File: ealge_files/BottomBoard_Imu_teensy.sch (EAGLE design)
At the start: 96 parts, among them K1 MK20DX256VLH7, K2 MKL04Z32VLC4, T1 MCP1825S, U2 MPU-9250

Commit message: completed bottom layer.. and started with nanopi shield
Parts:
- removed J2: (no value), SparkFun-Connectors:M04PTH
- removed MICRO-USB: MINI-USB, t32_ref:MINI-USBMOLEX_0675031230
- removed SX10, SX11, SX12, SX13, SX14, SX15, SX16, SX17, SX18, SX19, SX2, SX20, SX21, SX22, SX23, SX24, SX25, SX26, SX27, SX28, SX29, SX3, SX30, SX31, SX32, SX33, SX34, SX35, SX36, SX37, SX38, SX39, SX4, SX40, SX41, SX42, SX43, SX44, SX45, SX46, SX47, SX48, SX49, SX5, SX50, SX51, SX52, SX53, SX54, SX55, SX56, SX57, SX58, SX59, SX6, SX60, SX7, SX8, SX9: PIN, t32_ref:PIN
- added D1: GREEN, SparkFun-LED:LED-GREEN0603
- added FLEX-RIBBON: 52207-0485, Molex_By_element14_Batch_1:52207-0485
- added R1: 100, SparkFun-Resistors:100OHM-0603-1/4W-5%
- added S2: (no value), SparkFun-Switches:SWITCH-SPDT-SMD-RIGHT-ANGLE
- added U1: 52207-0885, Molex_By_element14_Batch_1:52207-0885
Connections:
- removed net N$12: K1.RESET_B, K2.PTA4, K2.PTB5, SX38.P$1, SX56.P$1
- removed net N$16: MICRO-USB.3, R10.1
- removed net N$17: MICRO-USB.2, R7.1
- removed net N$18: C11.1, MICRO-USB.1, R14.1
- removed net N$19: K1.PTA1, K2.PTA6, MICRO-USB.4
- removed net N$22: K1.PTC1, SX6.P$1
- removed net N$23: K1.PTD6, SX7.P$1
- removed net N$24: K1.PTD5, SX8.P$1
- removed net N$25: K1.PTB2, SX9.P$1
- removed net N$26: K1.PTB3, SX10.P$1
- removed net N$27: K1.PTB1, SX11.P$1
- removed net N$28: K1.PTB0, SX13.P$1
- removed net N$29: K1.PTC0, SX15.P$1
- removed net N$30: K1.PTD1, SX17.P$1
- removed net N$31: K1.PTC5, P1.+, SX18.P$1
- removed net N$32: K1.PTC7, SX19.P$1
- removed net N$33: K1.PTC6, SX20.P$1
- removed net N$34: K1.PTC4, SX21.P$1
- removed net N$35: K1.PTC3, SX22.P$1
- removed net N$36: K1.PTD3, SX23.P$1
- removed net N$37: K1.PTD2, SX24.P$1
- removed net N$38: K1.PTD4, SX25.P$1
- removed net N$39: K1.PTD7, SX26.P$1
- removed net N$40: K1.PTA13, SX27.P$1
- removed net N$41: K1.PTA12, SX28.P$1
- removed net N$42: K1.PTD0, SX29.P$1
- removed net N$43: K1.PTB17, SX30.P$1
- removed net N$44: K1.PTB16, SX31.P$1
- removed net N$45: K1.ADC0_DM3, SX33.P$1
- removed net N$46: K1.PTA4, SX35.P$1
- removed net N$47: K1.PTB18, SX36.P$1
- removed net N$48: K1.PTE0, SX37.P$1
- removed net N$49: K1.PTC11, SX39.P$1
- removed net N$50: K1.PTC10, SX41.P$1
- removed net N$51: K1.PTC8, SX43.P$1
- removed net N$54: K1.DAC0, SX52.P$1
- removed net N$55: K1.ADC0_DP3, SX51.P$1
- removed net N$57: K1.PTA5, SX49.P$1
- removed net N$58: K1.PTB19, SX48.P$1
- removed net N$59: K1.PTE1, SX47.P$1
- removed net N$60: K1.PTC9, SX45.P$1
- removed net N$63: R13.2, SX46.P$1
- removed net N$64: K1.ADC0_DM0, SX12.P$1
- removed net N$65: K1.ADC0_DP0, SX14.P$1
- removed net N$69: C10.1, C12.1, C5.1, C6.1, K1.VDD@3, K1.VDD@30, K1.VDD@48, K1.VOUT33, K2.VDD, K2.VREFH, R12.2, R13.1, SX34.P$1, SX4.P$1, SX44.P$1, SX54.P$1, T1.OUT
- new net ID: K1.PTA1, K2.PTA6, U1.4
- new net N$4: D1.C, R1.1
- new net USB_DM: R7.1, U1.2
- new net USB_DP: R10.1, U1.3
- new net VCC: C4.1, S2.O
- new net V_MICRO_USB: C11.1, R14.1, U1.1
- net GND: now also FLEX-RIBBON.4, FLEX-RIBBON.5, FLEX-RIBBON.6, R1.2, S2.S, U1.10, U1.5, U1.6, U1.7, U1.8, U1.9; no longer J2.4, MICRO-USB.5, MICRO-USB.CASE, SX32.P$1, SX42.P$1, SX50.P$1, SX53.P$1, SX55.P$1, SX60.P$1
- net N$1: now also K1.RESET_B, K2.PTA4, K2.PTB5; no longer K2.PTA3, SX59.P$1
- net N$13: no longer SX16.P$1
- net N$2: no longer SX58.P$1
- net N$21: now also K1.PTC5, P1.+; no longer K1.PTC2, SX5.P$1
- net N$53: no longer SX3.P$1
- net N$61: no longer SX2.P$1
- net N$70: no longer SX57.P$1
- net N$9: no longer SX40.P$1
- net SCL/SCLK: now also FLEX-RIBBON.2, K1.PTB2; no longer J2.1
- net SDA/SDI: now also FLEX-RIBBON.3, K1.PTB3; no longer J2.2
- net VDD: now also C10.1, C12.1, C5.1, C6.1, K1.VDD@3, K1.VDD@30, K1.VDD@48, K1.VOUT33, K2.VDD, K2.VREFH, R12.2, R13.1, T1.OUT; no longer C4.1, J2.3, U2.VDD, U2.VDDIO
- net VDDIO: now also D1.A, FLEX-RIBBON.1, S2.P, U2.VDD, U2.VDDIO
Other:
- note removed: "0"
- note removed: "1"
- note removed: "10"
- note removed: "11"
- note removed: "12"
- note removed: "14 / A0"
- note removed: "15 / A1"
- note removed: "16 / A2"
- note removed: "17 / A3"
- note removed: "2"
- note removed: "20 / A6"
- note removed: "21 / A7"
- note removed: "22 / A8"
- note removed: "23 / A9"
- note removed: "24"
- note removed: "25"
- note removed: "26"
- note removed: "27"
- note removed: "28"
- note removed: "29"
- note removed: "3"
- note removed: "30"
- note removed: "31"
- note removed: "32"
- note removed: "33"
- note removed: "4"
- note removed: "5"
- note removed: "6"
- note removed: "7"
- note removed: "8"
- note removed: "9"
- note removed: "A10"
- note removed: "A11"
- note removed: "A12"
- note removed: "A13"
- note removed: "AREF"
- note removed: "DAC / A14"
- note removed: "EN'"
- note removed: "GND"
- note removed: "PROG"
- note removed: "RESET"
- note removed: "SWC"
- note removed: "SWD"
- note removed: "VBAT"
- moved on the sheet: C11, C16, C3, C4, P1, R4, R5, R6, R9, SJ2, T1, U2

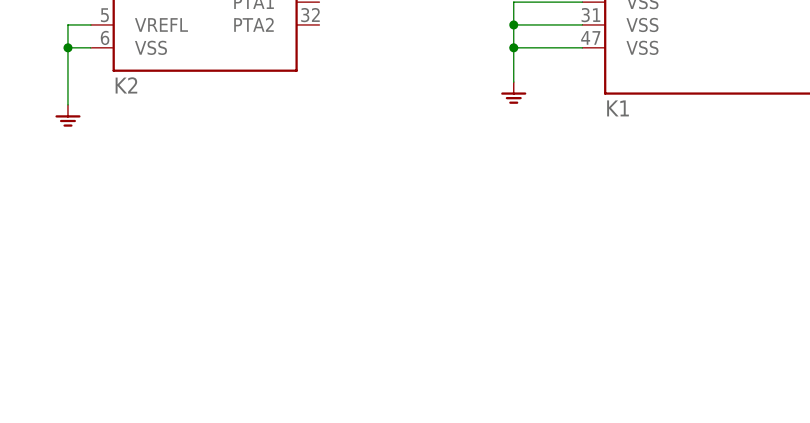
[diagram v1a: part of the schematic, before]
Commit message: added few libraries and completed all schematic
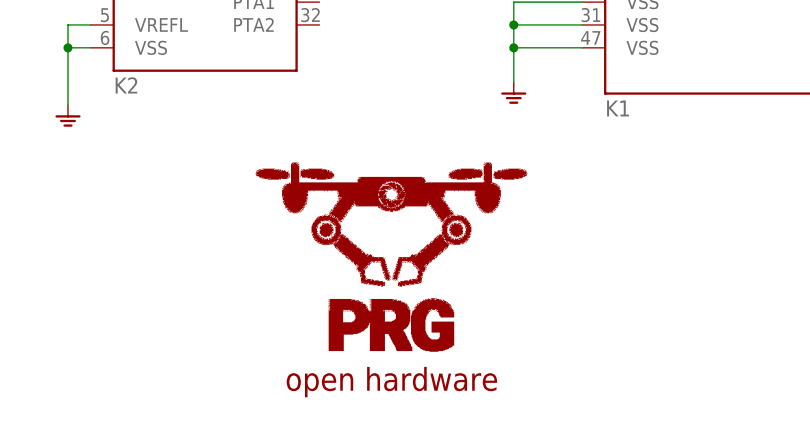
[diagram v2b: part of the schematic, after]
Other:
- note added: "open hardware"

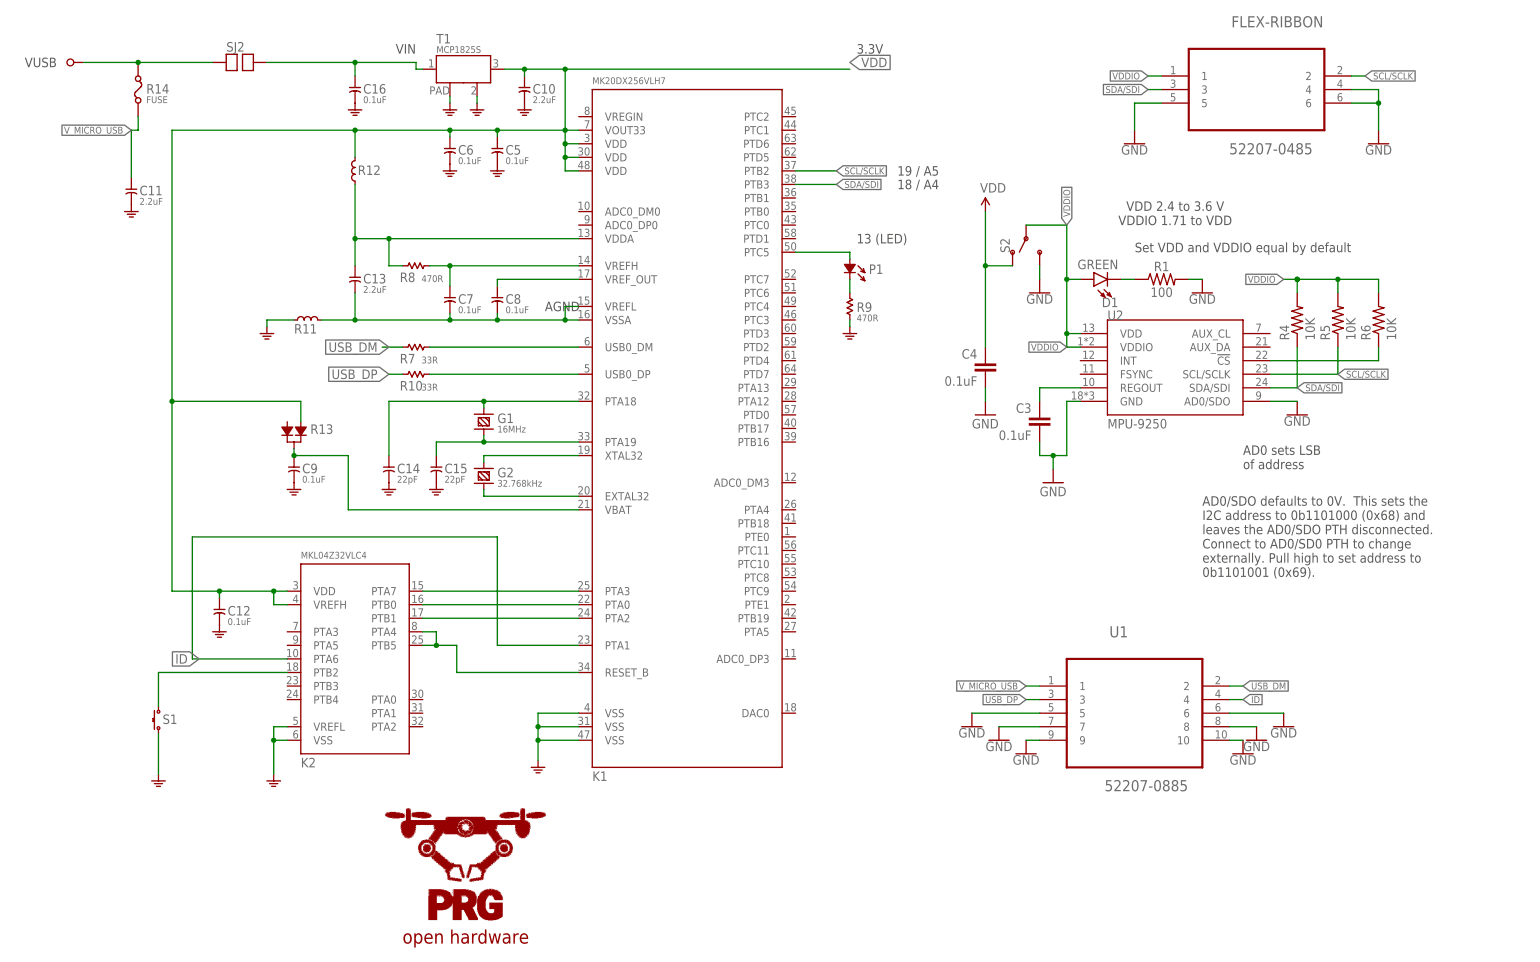
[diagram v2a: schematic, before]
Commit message: added molex for cam
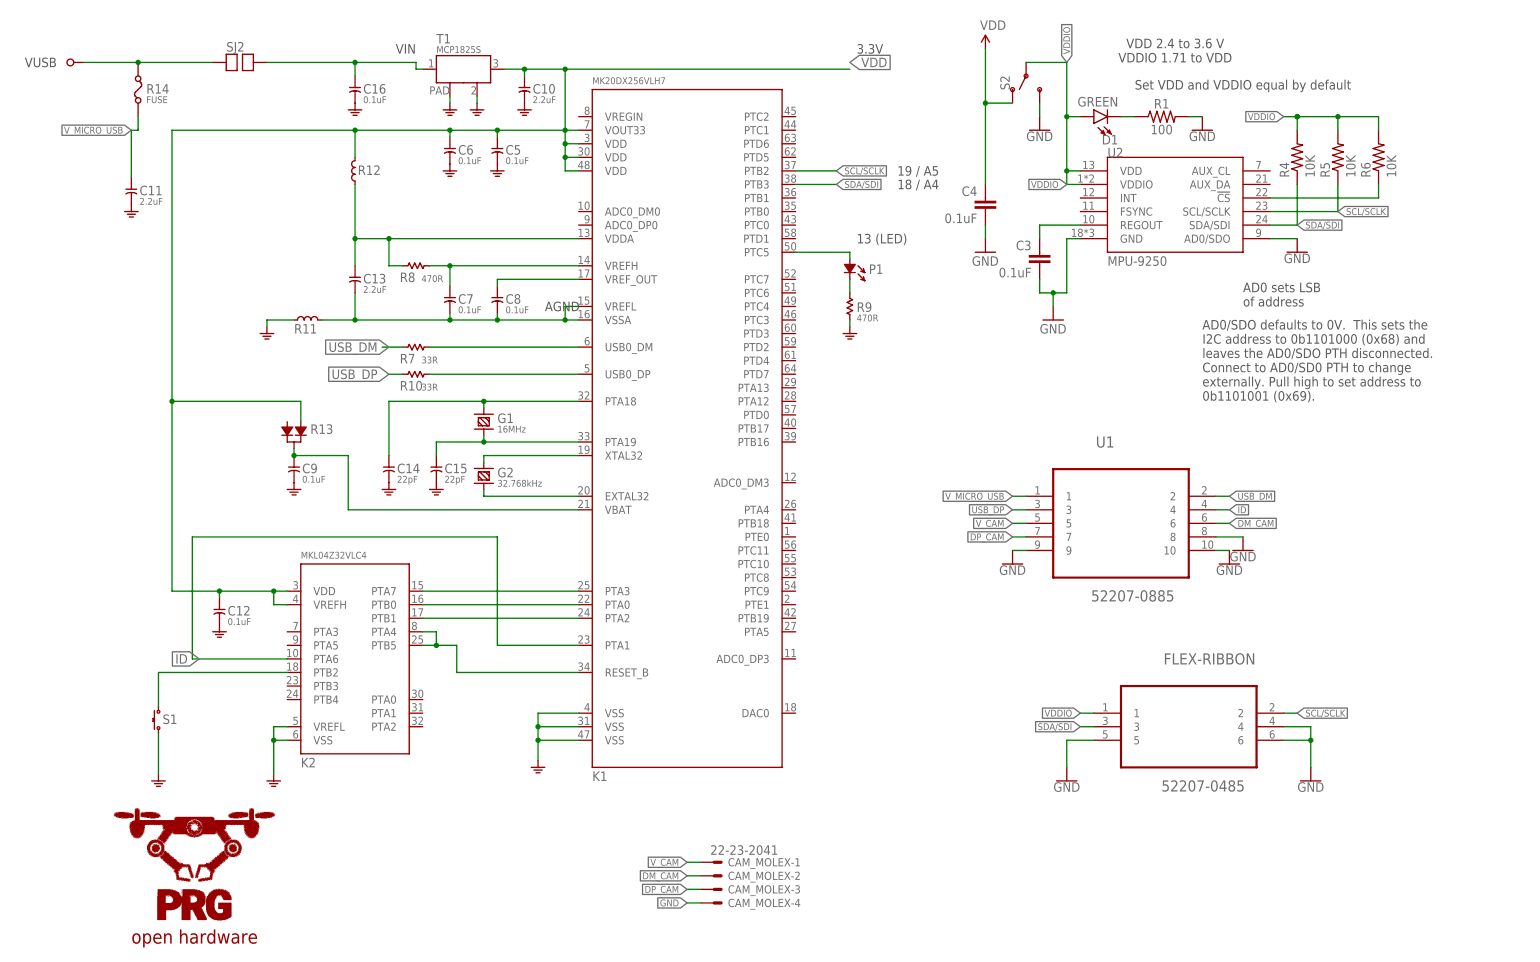
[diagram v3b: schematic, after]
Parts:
- added CAM_MOLEX: 22-23-2041, con-molex:22-23-2041
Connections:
- new net DM_CAM: CAM_MOLEX-2.S, U1.6
- new net DP_CAM: CAM_MOLEX-3.S, U1.7
- new net V_CAM: CAM_MOLEX-1.S, U1.5
- net GND: now also CAM_MOLEX-4.S; no longer U1.5, U1.6, U1.7
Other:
- moved on the sheet: C3, C4, D1, FLEX-RIBBON, R1, R4, R5, R6, S2, U1, U2
